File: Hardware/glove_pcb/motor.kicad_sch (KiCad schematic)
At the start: 5 parts, among them M1 Motor_DC, U2 DRV8848, U3 DRV8848, U4 DRV8848

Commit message: More work on motor driver connection
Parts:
- added C5: 0.1uF, symbol Device:C
- added C6: 10uF, symbol Device:C
- added C7: 2.2uF, symbol Device:C
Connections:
- net UC_MOTOR_SLEEP: now reaches U2.1 (nSLEEP)
- net at U2.11 (VREF): now also U2.14 (VINT), C7.2
- net MOTOR_VM: now reaches U2.12 (VM)
- net MOTOR_VM: now also C5.1, C6.1
- net GND: now reaches U2.13 (GND)
- net GND: now also U2.17 (PPAD), U2.3 (AISEN), U2.6 (BISEN), C5.2, C6.2, C7.1
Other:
- moved on the sheet: M1, U2

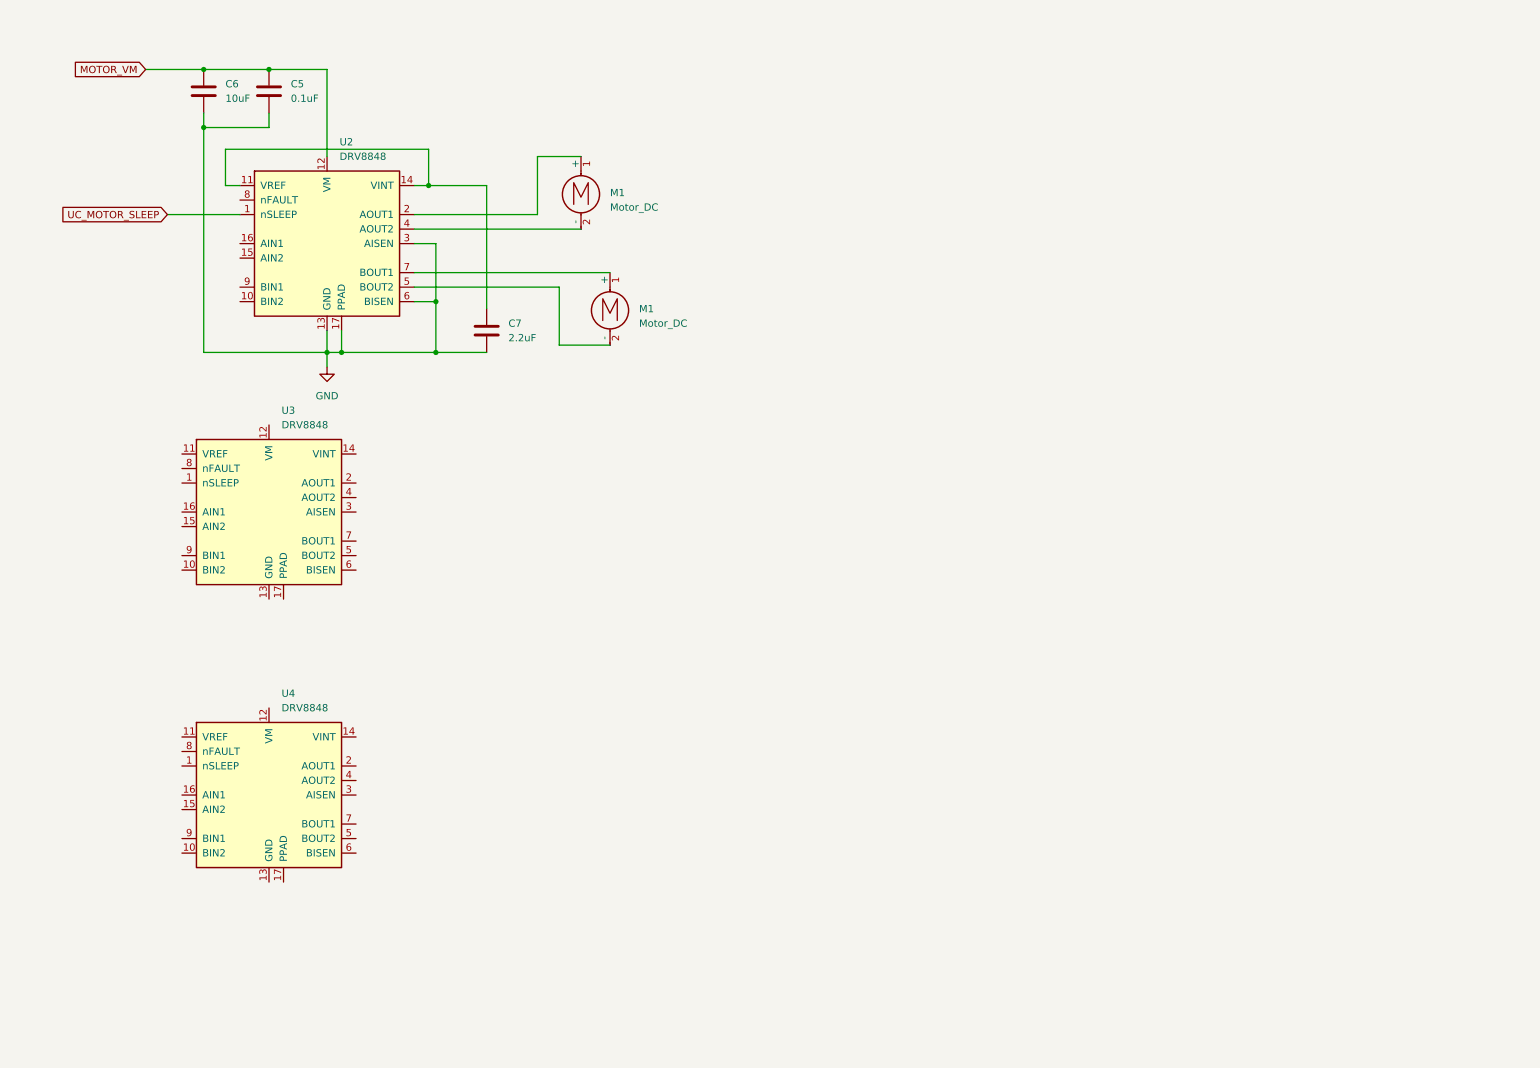
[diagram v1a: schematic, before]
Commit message: Add new dc motor driver
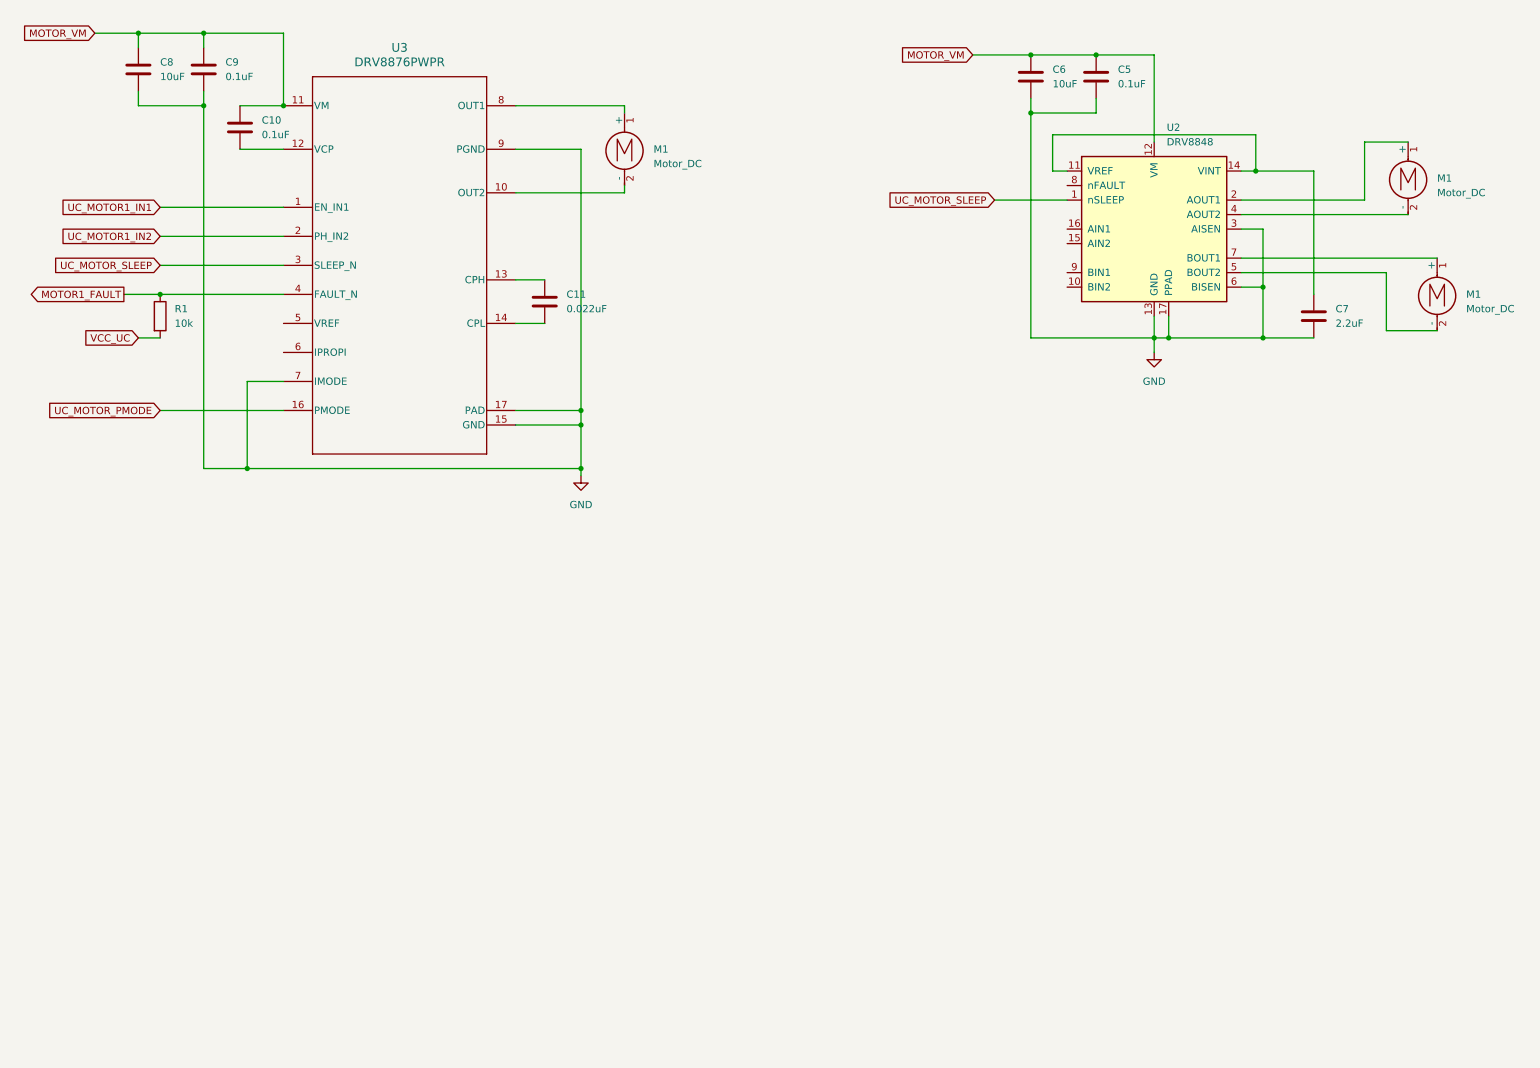
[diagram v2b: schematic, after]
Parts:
- removed U3, U4: DRV8848, Package_SO:TSSOP-16-1EP_4.4x5mm_P0.65mm, symbol Driver_Motor:DRV8848
- added C10, C9: 0.1uF, symbol Device:C
- added C11: 0.022uF, symbol Device:C
- added C8: 10uF, symbol Device:C
- added M1: Motor_DC, symbol Motor:Motor_DC
- added R1: 10k, symbol Device:R
- added U3: DRV8876PWPR, PWP0016J_N, symbol Glove_Symbols:DRV8876PWPR
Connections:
- net GND: now also C8.2, C9.2, U3.15 (GND), U3.17 (PAD), U3.7 (IMODE), U3.9 (PGND)
- net MOTOR_VM: now also C10.1, C8.1, C9.1, U3.11 (VM)
- net UC_MOTOR_SLEEP: now also U3.3 (SLEEP_N)
- new net: C11.1, U3.13 (CPH)
- new net: C11.2, U3.14 (CPL)
- new net: M1.2 (-), U3.10 (OUT2)
- new net: C10.2, U3.12 (VCP)
- new net: M1.1 (+), U3.8 (OUT1)
- new net MOTOR1_FAULT: R1.1, U3.4 (FAULT_N)
- new net UC_MOTOR1_IN1: U3.1 (EN_IN1)
- new net UC_MOTOR1_IN2: U3.2 (PH_IN2)
- new net UC_MOTOR_PMODE: U3.16 (PMODE)
- new net VCC_UC: R1.2
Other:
- moved on the sheet: C5, C6, C7, M1, U2

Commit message: Replace offboard components with connectors, add uC, add example mux, fix motor wiring
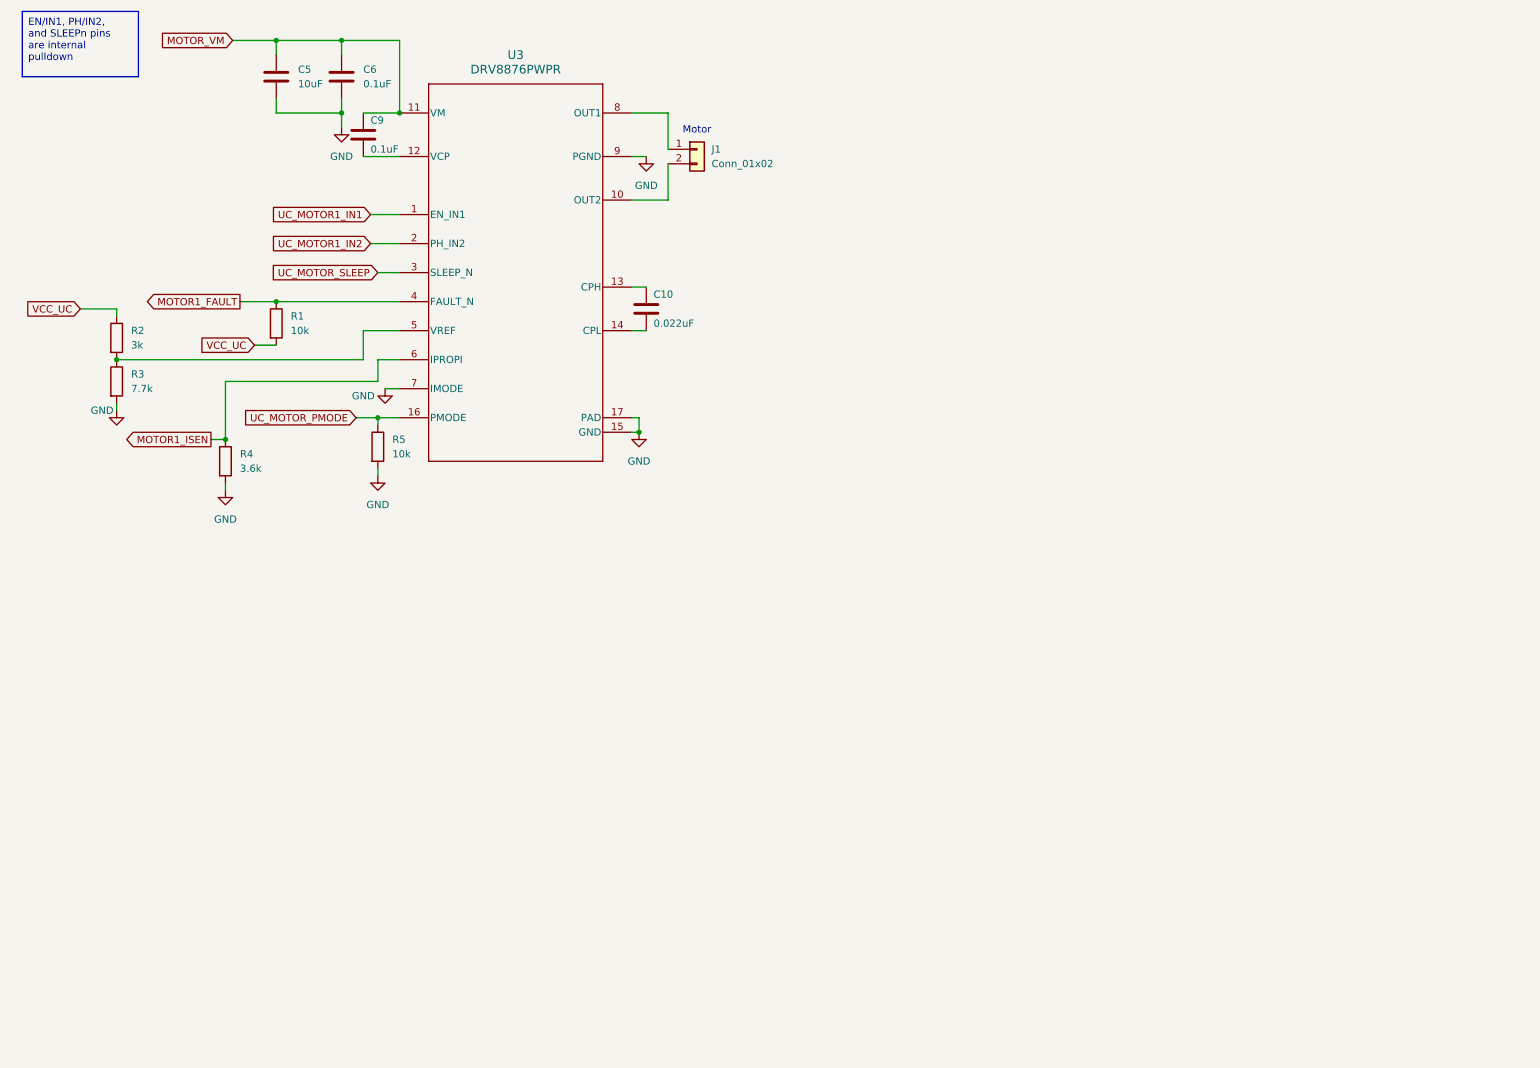
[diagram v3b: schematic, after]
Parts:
- removed C5: 0.1uF, symbol Device:C
- removed C6: 10uF, symbol Device:C
- removed C7: 2.2uF, symbol Device:C
- removed M1 (x3): Motor_DC, symbol Motor:Motor_DC
- removed U2: DRV8848, Package_SO:TSSOP-16-1EP_4.4x5mm_P0.65mm, symbol Driver_Motor:DRV8848
- added J1: Conn_01x02, symbol Connector_Generic:Conn_01x02
- added R2: 3k, symbol Device:R
- added R3: 7.7k, symbol Device:R
- added R4: 3.6k, symbol Device:R
- added R5: 10k, symbol Device:R
- renumbered C11 to C10, C8 to C5, C9 to C6, C10 to C9
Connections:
- net GND: now also R3.2, R4.2, R5.2
- net UC_MOTOR_PMODE: now also R5.1
- net VCC_UC: now also R2.1
- net at U3.10 (OUT2): now also J1.2 (Pin_2)
- net at U3.5 (VREF): now also R2.2, R3.1
- net MOTOR1_ISEN: now reaches U3.6 (IPROPI)
- net MOTOR1_ISEN: now also R4.1
- net at U3.8 (OUT1): now also J1.1 (Pin_1)
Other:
- note added: "Motor"
- moved on the sheet: C10, C5, C6, C9, R1, U3

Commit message: Minor changes from meeting with dmitry
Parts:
- C5: value 10uF -> 1000uF
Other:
- moved on the sheet: R1, R2, R3
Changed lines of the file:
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@@
 (kicad_sch (version 20230121) (generator eeschema)
-  (paper "A4")
-  (junction (at 33.02 77.47) (diameter 0) (color 0 0 0 0)
+  (paper "USLetter")
+  (junction (at 43.18 77.47) (diameter 0) (color 0 0 0 0)
   )
   (junction (at 124.46 90.17) (diameter 0) (color 0 0 0 0)
@@
   (junction (at 78.74 87.63) (diameter 0) (color 0 0 0 0)
   )
-  (junction (at 60.96 67.31) (diameter 0) (color 0 0 0 0)
+  (junction (at 68.58 67.31) (diameter 0) (color 0 0 0 0)
   )
   (junction (at 72.39 21.59) (diameter 0) (color 0 0 0 0)
@@
   (junction (at 82.55 34.29) (diameter 0) (color 0 0 0 0)
   )
-  (junction (at 72.39 34.29) (diameter 0) (color 0 0 0 0)
+  (junction (at 60.96 34.29) (diameter 0) (color 0 0 0 0)
   )
   (wire (pts (xy 60.96 21.59) (xy 60.96 24.13))
@@
     (stroke (width 0) (type default))
   )
-  (wire (pts (xy 54.61 67.31) (xy 60.96 67.31))
+  (wire (pts (xy 62.23 67.31) (xy 68.58 67.31))
     (stroke (width 0) (type default))
   )
@@
     (stroke (width 0) (type default))
   )
+  (wire (pts (xy 60.96 34.29) (xy 72.39 34.29))
+    (stroke (width 0) (type default))
+  )
   (wire (pts (xy 77.47 52.07) (xy 82.55 52.07))
     (stroke (width 0) (type default))
@@
     (stroke (width 0) (type default))
   )
-  (wire (pts (xy 33.02 85.09) (xy 33.02 86.36))
+  (wire (pts (xy 43.18 85.09) (xy 43.18 86.36))
     (stroke (width 0) (type default))
   )
@@
     (stroke (width 0) (type default))
   )
-  (wire (pts (xy 60.96 67.31) (xy 82.55 67.31))
-    (stroke (width 0) (type default))
-  )
-  (wire (pts (xy 33.02 77.47) (xy 76.2 77.47))
+  (wire (pts (xy 68.58 67.31) (xy 82.55 67.31))
+    (stroke (width 0) (type default))
+  )
+  (wire (pts (xy 43.18 77.47) (xy 76.2 77.47))
     (stroke (width 0) (type default))
   )
@@
     (stroke (width 0) (type default))
   )
-  (wire (pts (xy 57.15 74.93) (xy 60.96 74.93))
+  (wire (pts (xy 64.77 74.93) (xy 68.58 74.93))
     (stroke (width 0) (type default))
   )
@@
     (stroke (width 0) (type default))
   )
-  (wire (pts (xy 72.39 34.29) (xy 72.39 36.83))
-    (stroke (width 0) (type default))
-  )
-  (wire (pts (xy 26.67 68.58) (xy 33.02 68.58))
+  (wire (pts (xy 60.96 34.29) (xy 60.96 36.83))
+    (stroke (width 0) (type default))
+  )
+  (wire (pts (xy 40.64 68.58) (xy 43.18 68.58))
     (stroke (width 0) (type default))
   )
@@
     (stroke (width 0) (type default))
   )
-  (wire (pts (xy 33.02 68.58) (xy 33.02 69.85))
+  (wire (pts (xy 43.18 68.58) (xy 43.18 69.85))
     (stroke (width 0) (type default))
   )
@@
   )
   (wire (pts (xy 82.55 77.47) (xy 78.74 77.47))
-    (stroke (width 0) (type default))
-  )
-  (wire (pts (xy 60.96 34.29) (xy 72.39 34.29))
     (stroke (width 0) (type default))
   )
@@
     )
   )
-  (global_label "MOTOR1_FAULT" (shape output) (at 54.61 67.31 180) (fields_autoplaced)
-    (effects (font (size 1.27 1.27)) (justify right))
-    (property "Intersheetrefs" "${INTERSHEET_REFS}" (at 37.5943 67.31 0)
+  (global_label "MOTOR1_FAULT" (shape output) (at 62.23 67.31 180) (fields_autoplaced)
+    (effects (font (size 1.27 1.27)) (justify right))
+    (property "Intersheetrefs" "${INTERSHEET_REFS}" (at 45.2143 67.31 0)
       (effects (font (size 1.27 1.27)) (justify right) hide)
     )
@@
     )
   )
-  (global_label "VCC_UC" (shape input) (at 57.15 74.93 180) (fields_autoplaced)
-    (effects (font (size 1.27 1.27)) (justify right))
-    (property "Intersheetrefs" "${INTERSHEET_REFS}" (at 46.9681 74.93 0)
+  (global_label "VCC_UC" (shape input) (at 64.77 74.93 180) (fields_autoplaced)
+    (effects (font (size 1.27 1.27)) (justify right))
+    (property "Intersheetrefs" "${INTERSHEET_REFS}" (at 54.5881 74.93 0)
       (effects (font (size 1.27 1.27)) (justify right) hide)
     )
@@
     )
   )
-  (global_label "VCC_UC" (shape input) (at 26.67 68.58 180) (fields_autoplaced)
-    (effects (font (size 1.27 1.27)) (justify right))
-    (property "Intersheetrefs" "${INTERSHEET_REFS}" (at 16.4881 68.58 0)
-      (effects (font (size 1.27 1.27)) (justify right) hide)
-    )
-  )
-  (symbol (lib_id "power:GND") (at 72.39 36.83 0) (unit 1)
-    (in_bom yes) (on_board yes) (dnp no) (fields_autoplaced)
-    (property "Reference" "#PWR06" (at 72.39 43.18 0)
-      (effects (font (size 1.27 1.27)) hide)
-    )
-    (property "Value" "GND" (at 72.39 41.91 0)
+  (global_label "VCC_UC" (shape input) (at 40.64 68.58 180) (fields_autoplaced)
+    (effects (font (size 1.27 1.27)) (justify right))
+    (property "Intersheetrefs" "${INTERSHEET_REFS}" (at 30.4581 68.58 0)
+      (effects (font (size 1.27 1.27)) (justify right) hide)
+    )
+  )
+  (symbol (lib_id "power:GND") (at 60.96 36.83 0) (unit 1)
+    (in_bom yes) (on_board yes) (dnp no) (fields_autoplaced)
+    (property "Reference" "#PWR06" (at 60.96 43.18 0)
+      (effects (font (size 1.27 1.27)) hide)
+    )
+    (property "Value" "GND" (at 60.96 41.91 0)
       (effects (font (size 1.27 1.27)))
     )
-    (property "Footprint" "" (at 72.39 36.83 0)
-      (effects (font (size 1.27 1.27)) hide)
-    )
-    (property "Datasheet" "" (at 72.39 36.83 0)
+    (property "Footprint" "" (at 60.96 36.83 0)
+      (effects (font (size 1.27 1.27)) hide)
+    )
+    (property "Datasheet" "" (at 60.96 36.83 0)
       (effects (font (size 1.27 1.27)) hide)
     )
@@
   )
   (symbol (lib_id "Device:C") (at 60.96 27.94 0) (unit 1)
-    (in_bom yes) (on_board yes) (dnp no) (fields_autoplaced)
+    (in_bom yes) (on_board yes) (dnp no)
     (property "Reference" "C5" (at 64.77 26.67 0)
       (effects (font (size 1.27 1.27)) (justify left))
     )
-    (property "Value" "10uF" (at 64.77 29.21 0)
+    (property "Value" "1000uF" (at 63.5 30.48 0)
       (effects (font (size 1.27 1.27)) (justify left))
     )
@@
     )
   )
-  (symbol (lib_id "Device:R") (at 60.96 71.12 0) (unit 1)
-    (in_bom yes) (on_board yes) (dnp no) (fields_autoplaced)
-    (property "Reference" "R1" (at 63.5 69.85 0)
-      (effects (font (size 1.27 1.27)) (justify left))
-    )
-    (property "Value" "10k" (at 63.5 72.39 0)
-      (effects (font (size 1.27 1.27)) (justify left))
-    )
-    (property "Footprint" "" (at 59.182 71.12 90)
-      (effects (font (size 1.27 1.27)) hide)
-    )
-    (property "Datasheet" "~" (at 60.96 71.12 0)
+  (symbol (lib_id "Device:R") (at 68.58 71.12 0) (unit 1)
+    (in_bom yes) (on_board yes) (dnp no) (fields_autoplaced)
+    (property "Reference" "R1" (at 71.12 69.85 0)
+      (effects (font (size 1.27 1.27)) (justify left))
+    )
+    (property "Value" "10k" (at 71.12 72.39 0)
+      (effects (font (size 1.27 1.27)) (justify left))
+    )
+    (property "Footprint" "" (at 66.802 71.12 90)
+      (effects (font (size 1.27 1.27)) hide)
+    )
+    (property "Datasheet" "~" (at 68.58 71.12 0)
       (effects (font (size 1.27 1.27)) hide)
     )
@@
     )
   )
-  (symbol (lib_id "Device:R") (at 33.02 73.66 0) (unit 1)
-    (in_bom yes) (on_board yes) (dnp no) (fields_autoplaced)
-    (property "Reference" "R2" (at 35.56 72.39 0)
-      (effects (font (size 1.27 1.27)) (justify left))
-    )
-    (property "Value" "3k" (at 35.56 74.93 0)
-      (effects (font (size 1.27 1.27)) (justify left))
-    )
-    (property "Footprint" "" (at 31.242 73.66 90)
-      (effects (font (size 1.27 1.27)) hide)
-    )
-    (property "Datasheet" "~" (at 33.02 73.66 0)
+  (symbol (lib_id "Device:R") (at 43.18 73.66 0) (unit 1)
+    (in_bom yes) (on_board yes) (dnp no) (fields_autoplaced)
+    (property "Reference" "R2" (at 45.72 72.39 0)
+      (effects (font (size 1.27 1.27)) (justify left))
+    )
+    (property "Value" "3k" (at 45.72 74.93 0)
+      (effects (font (size 1.27 1.27)) (justify left))
+    )
+    (property "Footprint" "" (at 41.402 73.66 90)
+      (effects (font (size 1.27 1.27)) hide)
+    )
+    (property "Datasheet" "~" (at 43.18 73.66 0)
       (effects (font (size 1.27 1.27)) hide)
     )
@@
     )
   )
-  (symbol (lib_id "power:GND") (at 33.02 86.36 0) (unit 1)
+  (symbol (lib_id "power:GND") (at 43.18 86.36 0) (unit 1)
     (in_bom yes) (on_board yes) (dnp no)
-    (property "Reference" "#PWR010" (at 33.02 92.71 0)
-      (effects (font (size 1.27 1.27)) hide)
-    )
-    (property "Value" "GND" (at 30.48 86.36 0)
+    (property "Reference" "#PWR010" (at 43.18 92.71 0)
+      (effects (font (size 1.27 1.27)) hide)
+    )
+    (property "Value" "GND" (at 40.64 86.36 0)
       (effects (font (size 1.27 1.27)))
     )
-    (property "Footprint" "" (at 33.02 86.36 0)
-      (effects (font (size 1.27 1.27)) hide)
-    )
-    (property "Datasheet" "" (at 33.02 86.36 0)
+    (property "Footprint" "" (at 43.18 86.36 0)
+      (effects (font (size 1.27 1.27)) hide)
+    )
+    (property "Datasheet" "" (at 43.18 86.36 0)
       (effects (font (size 1.27 1.27)) hide)
     )
@@
     )
   )
-  (symbol (lib_id "Device:R") (at 33.02 81.28 0) (unit 1)
-    (in_bom yes) (on_board yes) (dnp no) (fields_autoplaced)
-    (property "Reference" "R3" (at 35.56 80.01 0)
-      (effects (font (size 1.27 1.27)) (justify left))
-    )
-    (property "Value" "7.7k" (at 35.56 82.55 0)
-      (effects (font (size 1.27 1.27)) (justify left))
-    )
-    (property "Footprint" "" (at 31.242 81.28 90)
-      (effects (font (size 1.27 1.27)) hide)
-    )
-    (property "Datasheet" "~" (at 33.02 81.28 0)
-      (effects (font (size 1.27 1.27)) hide)
-    )
+  (symbol (lib_id "Device:R") (at 43.18 81.28 0) (unit 1)
+    (in_bom yes) (on_board yes) (dnp no) (fields_autoplaced)
+    (property "Reference" "R3" (at 45.72 80.01 0)
+      (effects (font (size 1.27 1.27)) (justify left))
+    )
+    (property "Value" "7.7k" (at 45.72 82.55 0)
+      (effects (font (size 1.27 1.27)) (justify left))
+    )
+    (property "Footprint" "" (at 41.402 81.28 90)
+      (effects (font (size 1.27 1.27)) hide)
+    )
+    (property "Datasheet" "~" (at 43.18 81.28 0)
+      (effects (font (size 1.27 1.27)) hide)
+    )

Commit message: Yet more improvements to the schematic
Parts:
- C5: value 1000uF -> 1mF
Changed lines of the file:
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@@
       (effects (font (size 1.27 1.27)) (justify left))
     )
-    (property "Value" "1000uF" (at 63.5 30.48 0)
+    (property "Value" "1mF" (at 64.77 29.21 0)
       (effects (font (size 1.27 1.27)) (justify left))
     )
